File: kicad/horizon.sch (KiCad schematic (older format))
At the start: 105 parts, among them J1 OLED, SW1 SW_Push, SW10 SW_Push, SW11 SW_Push, SW12 SW_Push, SW13 SW_Push, SW14 SW_Push, SW15 SW_Push, SW16 SW_Push, SW17 SW_Push, SW18 SW_Push, SW19 SW_Push, SW2 SW_Push, SW20 SW_Push, SW21 SW_Push, SW22 SW_Push, SW23 SW_Push, SW24 SW_Push, SW25 SW_Push, SW26 SW_Push, SW27 SW_Push, SW28 SW_Push, SW29 SW_Push, SW3 SW_Push, SW30 SW_Push, SW31 SW_Push, SW32 SW_Push, SW33 SW_Push, SW34 SW_Push, SW35 SW_Push, SW36 SW_Push, SW37 SW_Push, SW38 SW_Push, SW39 SW_Push, SW4 SW_Push, SW40 SW_Push, SW41 SW_Push, SW42 SW_Push, SW5 SW_Push, SW6 SW_Push, SW7 SW_Push, SW8 SW_Push, SW9 SW_Push, U1 PRO-MICRO

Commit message: Begin revision 2
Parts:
- removed H10, H11, H12, H13, H14, H15, H9: Hole_Pad, horizon-footprints:MountingHole_M2, symbol horizon-components:Hole_Pad
- removed R1, R2: R, horizon-footprints:R_0805, symbol horizon-components:R
- D1, D10, D11, D12, D13, D14, D15, D16, D17, D18, D19, D2, D20, D21, D22, D23, D24, D25, D26, D27, D28, D29, D3, D30, D31, D32, D33, D34, D35, D36, D37, D38, D39, D4, D40, D41, D42, D5, D6, D7, D8, D9: footprint horizon-footprints:D_SOD-323 -> horizon-footprints:D_SOD-123
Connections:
- net COL1: now also U1.7 (4/PD4); no longer U1.20 (A3/PF4)
- net COL2: now also U1.8 (5/PC6); no longer U1.19 (A2/PF5)
- net COL3: now also U1.9 (6/PD7); no longer U1.18 (A1/PF6)
- net COL4: now also U1.10 (7/PE6); no longer U1.17 (A0/PF7)
- net COL5: now also U1.11 (8/PB4); no longer U1.16 (15/PB1)
- net COL6: now also U1.12 (9/PB5); no longer U1.15 (14/PB3)
- net ROW1: now also U1.19 (A2/PF5); no longer U1.14 (16/PB2)
- net ROW2: now also U1.16 (15/PB1); no longer U1.13 (10/PB6)
- net ROW3: now also U1.18 (A1/PF6); no longer U1.8 (5/PC6)
- net ROW4: now also U1.15 (14/PB3); no longer U1.9 (6/PD7)
- net ROW5: now also U1.17 (A0/PF7); no longer U1.10 (7/PE6)
- net ROW6: now also U1.14 (16/PB2); no longer U1.11 (8/PB4)
- net ROW7: now also U1.13 (10/PB6); no longer U1.12 (9/PB5)
- no-connect marks 19 -> 12

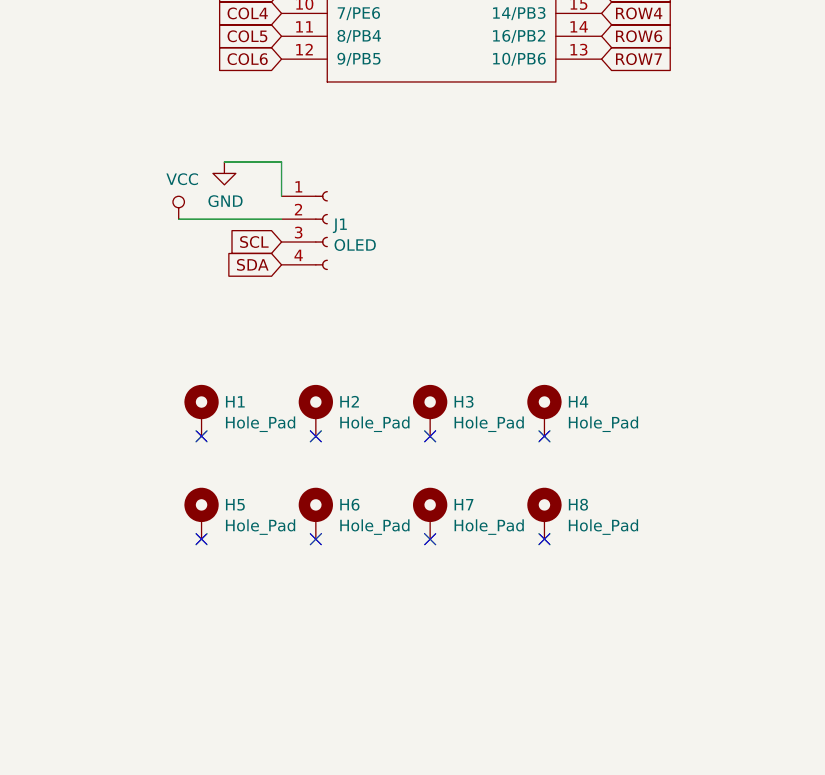
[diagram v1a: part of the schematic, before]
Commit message: Create bottom plate board. Begin laying out Choc switch board. Clean up footprints and remove unused ones
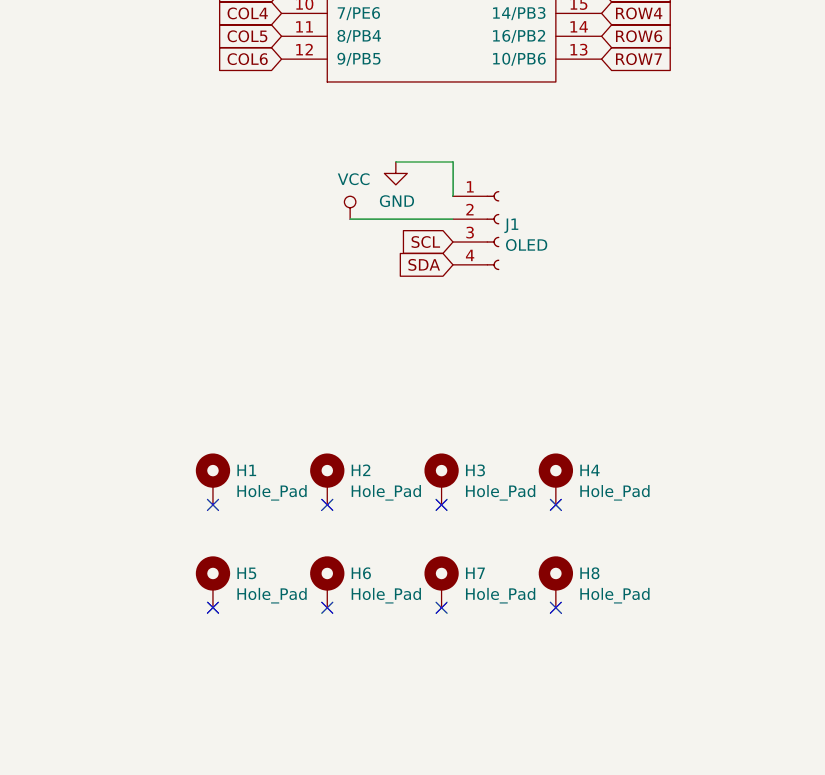
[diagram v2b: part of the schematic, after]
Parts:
- H1, H2, H3, H4, H5, H6, H7, H8: footprint horizon-footprints:MountingHole_M2 -> horizon-footprints:Mount_M2
- J1: footprint horizon-footprints:Header_THT_1x04_2.54mm -> horizon-footprints:Header_1x04_2.54mm
- TSW1: footprint horizon-footprints:SW_PUSH_6mm -> horizon-footprints:SW_Push_6mm
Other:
- moved on the sheet: H1, H2, H3, H4, H5, H6, H7, H8, J1
